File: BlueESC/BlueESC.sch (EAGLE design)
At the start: 36 parts, among them U1 ATMEGA168, U2 V_REG_LDOSMD, Y1 RESONATORSMD

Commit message: Combined logic and power boards into a single board. This is done for several reasons. The first is to create a consistent single schematic to help others view the design. The second is for manufacturing and avoiding double cost of setup.
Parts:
- added C10: 0.1uF, SparkFun-Capacitors:CAP0603-CAP
- added C11, C15, C16, C17: 100uF, SparkFun-Capacitors:CAP_POL7343
- added C2, C3: 1uF, SparkFun-Capacitors:CAP0805
- added C6: 1uF, SparkFun-Capacitors:CAP0603-CAP
- added D1, D2, D3: Schottky, SparkFun-DiscreteSemi:DIODESOD
- added Q1, Q2, Q3: BC817-40W, SparkFun-DiscreteSemi:TRANSISTOR_NPNSOT23
- added Q4, Q5, Q6, Q7, Q8, Q9: SI7370, transistor-fet-bobstarr:SI7370
- added R19, R21, R25, R26, R30, R31: 100, SparkFun-Resistors:33KOHM1/10W1%(0603)
- added R20: 3.3K 1%, SparkFun-Resistors:33KOHM1/10W1%(0603)
- added R22, R27, R32: 10K, SparkFun-Resistors:33KOHM1/10W1%(0603)
- added R23, R28: 2.2K, SparkFun-Resistors:33KOHM1/10W1%(0603)
- added R24, R29: 4.7K, SparkFun-Resistors:33KOHM1/10W1%(0603)
- added R33: 10K NTC, SparkFun-Resistors:33KOHM1/10W1%(0603)
- added R34: 47K, SparkFun:RESISTOR0603-RES
- added R35: 470K, SparkFun:RESISTOR0603-RES
- added U$1, U$2: PADPTH-MED, BR-Eagle-Library:PADPTH-MED
- added U$12, U$13, U$14: PAD1.5X3MM, BR-Eagle-Library:PAD1.5X3MM
- added U$5, U$6, U$7: PAD18AWG, BR-Eagle-Library:PAD18AWG
- added U$8: HEADER-122MM, BR-Eagle-Library:HEADER-122MM
- C1: device SparkFun-Capacitors:CAP0603-CAP -> SparkFun-Capacitors:CAP0805
- R17: value 47K -> 2.2K; device SparkFun:RESISTOR0603-RES -> SparkFun-Resistors:33KOHM1/10W1%(0603)
- R18: value 470K -> 4.7K; device SparkFun:RESISTOR0603-RES -> SparkFun-Resistors:33KOHM1/10W1%(0603)
- U$10: value PAD1.5X3MM -> LOGOBR-LOGO-M; device BR-Eagle-Library:PAD1.5X3MM -> BR-Eagle-Library:LOGOBR-LOGO-M
- U$3: value PAD1.5X3MM -> ACS7XX12-WFQFN; device BR-Eagle-Library:PAD1.5X3MM -> BR-Eagle-Library:ACS7XX12-WFQFN
- U$4: value LOGOBR-LOGO-M -> HEADER-62MM; device BR-Eagle-Library:LOGOBR-LOGO-M -> BR-Eagle-Library:HEADER-62MM
- U$9: value PAD1.5X3MM -> LOGOBR-LOGO-S; device BR-Eagle-Library:PAD1.5X3MM -> BR-Eagle-Library:LOGOBR-LOGO-S
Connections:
- new net GATE_AH: Q4.G, R19.2
- new net GATE_AL: Q5.G, R21.2, R22.2
- new net GATE_BH: Q6.G, R25.2
- new net GATE_BL: Q7.G, R26.2, R27.2
- new net GATE_CH: Q8.G, R30.2
- new net GATE_CL: Q9.G, R31.2, R32.2
- new net L_CURRENT_ADC: R34.1, U$17.4
- new net L_GND: C4.2, C5.2, C6.2, C7.2, C9.-, LED2.C, R11.1, R35.1, R7.1, R8.1, R9.1, U$11.PAD, U$16.1, U$17.1, U$17.12, U$17.2, U1.AGND, U1.GND@1, U1.GND@2, U2.GND, Y1.2
- new net L_PHASE_A: R4.2, U$16.2
- new net L_PHASE_B: R5.2, U$16.3
- new net L_PHASE_C: R6.2, U$16.4
- new net L_PWM_AH: U$17.5, U1.PD2(INT0)
- new net L_PWM_AL: U$17.6, U1.PD3(INT1)
- new net L_PWM_BH: U$17.7, U1.PD4(XCK/T0)
- new net L_PWM_BL: U$17.8, U1.PD5(T1)
- new net L_PWM_CH: U$17.9, U1.PD7(AIN1)
- new net L_PWM_CL: U$17.10, U1.PB3(MOSI/OC2)
- new net L_TEMP_ADC: U$16.5, U1.ADC7
- new net L_VBAT: R10.2, U$17.11, U2.IN
- new net N$12: C3.1, D1.C, R17.2
- new net N$15: C1.1, D2.C, R23.2
- new net N$19: C2.1, D3.C, R28.2
- new net N$2: Q1.B, R18.2
- new net N$4: Q1.C, R17.1, R19.1
- new net N$5: Q2.B, R24.2
- new net N$6: Q2.C, R23.1, R25.1
- new net N$7: Q3.B, R29.2
- new net N$9: Q3.C, R28.1, R30.1
- new net VBAT+: C11.+, C15.+, C16.+, C17.+, U$1.PAD, U$3.IP+1, U$3.IP+2
- new net VCC5V-1: R20.2, U$4.6
- new net VCC5V-2: C10.1, U$3.VCC, U$8.3
- net CURRENT_ADC: now also U$3.VIOUT, U$8.4; no longer R17.1, U$17.4
- net CURRENT_ADC_FILTERED: now also C6.1, R34.2; no longer C1.1, R17.2
- net GND: now also C10.2, C11.-, C15.-, C16.-, C17.-, Q1.E, Q2.E, Q3.E, Q5.S3, Q7.S3, Q9.S3, R22.1, R27.1, R32.1, R33.1, U$2.PAD, U$3.GND, U$4.1, U$8.1, U$8.12, U$8.2; no longer C1.2, C4.2, C5.2, C7.2, C9.-, LED2.C, R11.1, R18.1, R7.1, R8.1, R9.1, U$16.1, U$17.1, U$17.12, U$17.2, U$3.PAD, U1.AGND, U1.GND@1, U1.GND@2, U2.GND, Y1.2
- net PHASE_A: now also C3.2, Q4.S3, Q5.D, U$4.2, U$5.PAD; no longer R4.2, U$16.2
- net PHASE_B: now also C1.2, Q6.S3, Q7.D, U$4.3, U$6.PAD; no longer R5.2, U$16.3
- net PHASE_C: now also C2.2, Q8.S3, Q9.D, U$4.4, U$7.PAD; no longer R6.2, U$16.4
- net PWM: now also R35.2, U$14.PAD; no longer R18.2, U$11.PAD
- net PWM_AH: now also R18.1, U$8.5; no longer U$17.5, U1.PD2(INT0)
- net PWM_AL: now also R21.1, U$8.6; no longer U$17.6, U1.PD3(INT1)
- net PWM_BH: now also R24.1, U$8.7; no longer U$17.7, U1.PD4(XCK/T0)
- net PWM_BL: now also R26.1, U$8.8; no longer U$17.8, U1.PD5(T1)
- net PWM_CH: now also R29.1, U$8.9; no longer U$17.9, U1.PD7(AIN1)
- net PWM_CL: now also R31.1, U$8.10; no longer U$17.10, U1.PB3(MOSI/OC2)
- net SCL: now also U$13.PAD; no longer U$10.PAD
- net SDA: now also U$12.PAD; no longer U$9.PAD
- net TEMP_ADC: now also R20.1, R33.2, U$4.5; no longer U$16.5, U1.ADC7
- net VBAT: now also D1.A, D2.A, D3.A, Q4.D, Q6.D, Q8.D, U$3.IP-1, U$3.IP-2, U$8.11; no longer R10.2, U$17.11, U2.IN
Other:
- note added: "Current Sense"
- note added: "Interface between top and bottom board (ignore for now)"
- note added: "MOSFET Driving"
- note added: "MOSFETs"
- note added: "Motor Pads"
- note added: "Power Decoupling"
- note added: "Power Pads"
- note added: "Temperature Sense"

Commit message: Reorganized combined schematic and broke everything into multiple sheets for easier viewing.
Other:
- note added: "Connections"
- note added: "Control Interface"
- note added: "Current/Voltage/Temp Sensing"
- note added: "Logic Board"
- note added: "Microcontroller"
- note added: "Power"
- note added: "Power Board"
- note removed: "Interface"
- note removed: "Interface between top and bottom board (ignore for now)"
- note removed: "MCU"

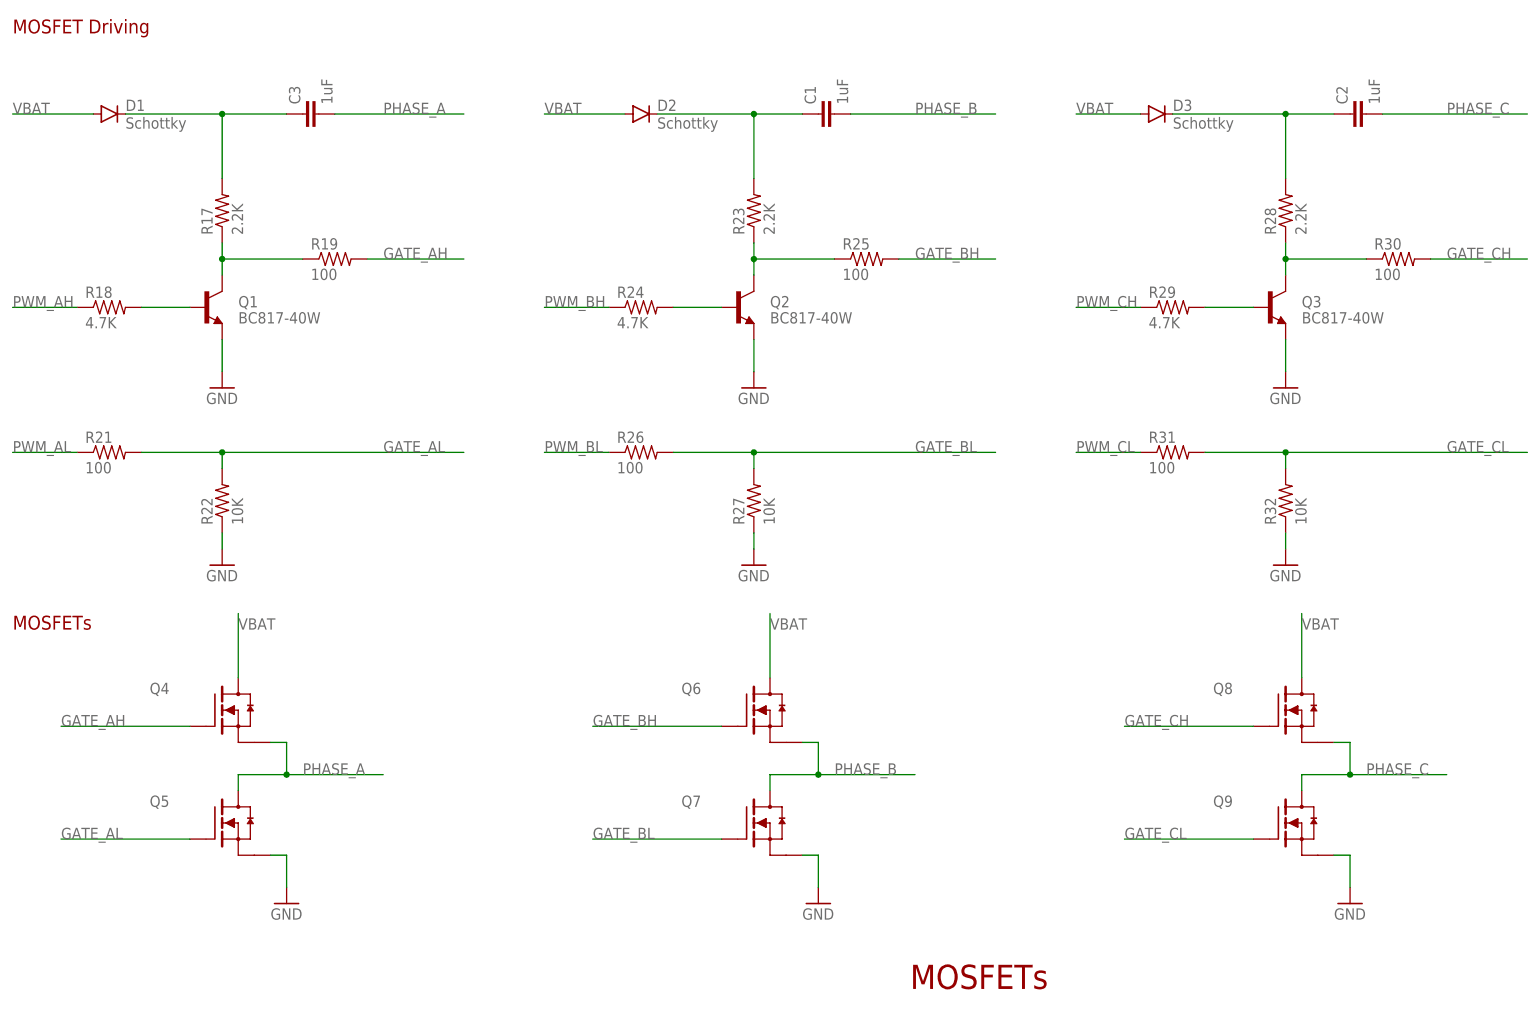
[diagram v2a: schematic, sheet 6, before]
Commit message: Updated MOSFET footprint to TDSON-8 to accommodate new FET and to fix potential soldering errors. This should still fit the SiR158DP as well.
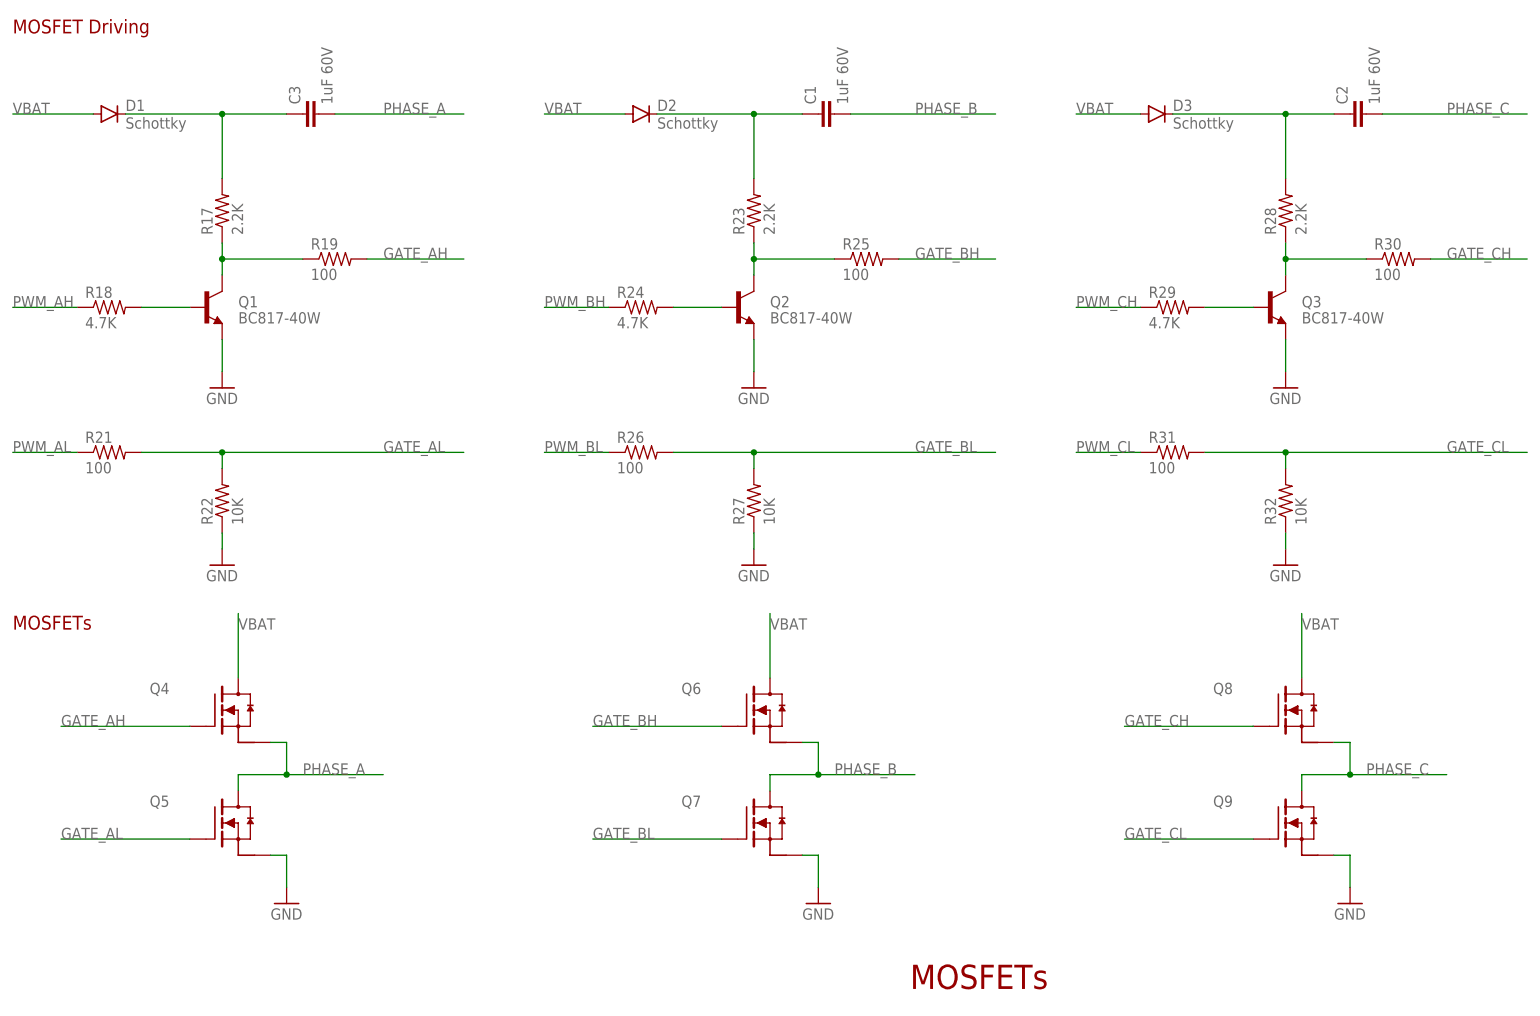
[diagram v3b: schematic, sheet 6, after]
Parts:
- C1, C2, C3: value 1uF -> 1uF 60V
- Q4, Q5, Q6, Q7, Q8, Q9: value SI7370 -> MOSFET-NCHANNEL; device transistor-fet-bobstarr:SI7370 -> BlueRobotics-Main:MOSFET-NCHANNEL
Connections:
- net GND: now also Q5.S, Q7.S, Q9.S; no longer Q5.S3, Q7.S3, Q9.S3
- net PHASE_A: now also Q4.S; no longer Q4.S3
- net PHASE_B: now also Q6.S; no longer Q6.S3
- net PHASE_C: now also Q8.S; no longer Q8.S3
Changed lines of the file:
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@@
 <part name="R32" library="SparkFun-Resistors" deviceset="33KOHM1/10W1%(0603)" device="" value="10K"/>
 <part name="GND16" library="SparkFun" deviceset="GND" device=""/>
-<part name="Q4" library="transistor-fet-bobstarr" deviceset="SI7370" device=""/>
-<part name="Q5" library="transistor-fet-bobstarr" deviceset="SI7370" device=""/>
+<part name="Q4" library="BlueRobotics-Main" deviceset="MOSFET-NCHANNEL" device=""/>
+<part name="Q5" library="BlueRobotics-Main" deviceset="MOSFET-NCHANNEL" device=""/>
 <part name="GND18" library="SparkFun-Aesthetics" deviceset="GND" device=""/>
-<part name="Q6" library="transistor-fet-bobstarr" deviceset="SI7370" device=""/>
-<part name="Q7" library="transistor-fet-bobstarr" deviceset="SI7370" device=""/>
+<part name="Q6" library="BlueRobotics-Main" deviceset="MOSFET-NCHANNEL" device=""/>
+<part name="Q7" library="BlueRobotics-Main" deviceset="MOSFET-NCHANNEL" device=""/>
 <part name="GND19" library="SparkFun-Aesthetics" deviceset="GND" device=""/>
-<part name="Q8" library="transistor-fet-bobstarr" deviceset="SI7370" device=""/>
-<part name="Q9" library="transistor-fet-bobstarr" deviceset="SI7370" device=""/>
+<part name="Q8" library="BlueRobotics-Main" deviceset="MOSFET-NCHANNEL" device=""/>
+<part name="Q9" library="BlueRobotics-Main" deviceset="MOSFET-NCHANNEL" device=""/>
 <part name="GND20" library="SparkFun-Aesthetics" deviceset="GND" device=""/>
 <part name="C15" library="SparkFun-Capacitors" deviceset="CAP_POL" device="7343" value="100uF"/>
@@
 <part name="D2" library="SparkFun-DiscreteSemi" deviceset="DIODE" device="SOD" value="Schottky"/>
 <part name="D3" library="SparkFun-DiscreteSemi" deviceset="DIODE" device="SOD" value="Schottky"/>
-<part name="C1" library="SparkFun-Capacitors" deviceset="CAP" device="0805" value="1uF"/>
-<part name="C2" library="SparkFun-Capacitors" deviceset="CAP" device="0805" value="1uF"/>
-<part name="C3" library="SparkFun-Capacitors" deviceset="CAP" device="0805" value="1uF"/>
+<part name="C1" library="SparkFun-Capacitors" deviceset="CAP" device="0805" value="1uF 60V"/>
+<part name="C2" library="SparkFun-Capacitors" deviceset="CAP" device="0805" value="1uF 60V"/>
+<part name="C3" library="SparkFun-Capacitors" deviceset="CAP" device="0805" value="1uF 60V"/>
 <part name="GND2" library="SparkFun-Aesthetics" deviceset="GND" device=""/>
 <part name="C10" library="SparkFun-Capacitors" deviceset="CAP" device="0603-CAP" value="0.1uF"/>
@@
 <net name="GND" class="0">
 <segment>
-<pinref part="Q5" gate="G$1" pin="S3"/>
+<pinref part="Q5" gate="G$1" pin="S"/>
 <pinref part="GND18" gate="1" pin="GND"/>
 <wire x1="48.26" y1="48.26" x2="50.8" y2="48.26" width="0.1524" layer="91"/>
@@
 </segment>
 <segment>
-<pinref part="Q7" gate="G$1" pin="S3"/>
+<pinref part="Q7" gate="G$1" pin="S"/>
 <pinref part="GND19" gate="1" pin="GND"/>
 <wire x1="132.08" y1="48.26" x2="134.62" y2="48.26" width="0.1524" layer="91"/>
@@
 </segment>
 <segment>
-<pinref part="Q9" gate="G$1" pin="S3"/>
+<pinref part="Q9" gate="G$1" pin="S"/>
 <pinref part="GND20" gate="1" pin="GND"/>
 <wire x1="215.9" y1="48.26" x2="218.44" y2="48.26" width="0.1524" layer="91"/>
@@
 <wire x1="43.18" y1="58.42" x2="43.18" y2="60.96" width="0.1524" layer="91"/>
 <wire x1="43.18" y1="60.96" x2="50.8" y2="60.96" width="0.1524" layer="91"/>
-<pinref part="Q4" gate="G$1" pin="S3"/>
+<pinref part="Q4" gate="G$1" pin="S"/>
 <wire x1="50.8" y1="60.96" x2="66.04" y2="60.96" width="0.1524" layer="91"/>
 <wire x1="48.26" y1="66.04" x2="50.8" y2="66.04" width="0.1524" layer="91"/>
@@
 <wire x1="127" y1="58.42" x2="127" y2="60.96" width="0.1524" layer="91"/>
 <wire x1="127" y1="60.96" x2="134.62" y2="60.96" width="0.1524" layer="91"/>
-<pinref part="Q6" gate="G$1" pin="S3"/>
+<pinref part="Q6" gate="G$1" pin="S"/>
 <wire x1="134.62" y1="60.96" x2="149.86" y2="60.96" width="0.1524" layer="91"/>
 <wire x1="132.08" y1="66.04" x2="134.62" y2="66.04" width="0.1524" layer="91"/>
@@
 <wire x1="210.82" y1="58.42" x2="210.82" y2="60.96" width="0.1524" layer="91"/>
 <wire x1="210.82" y1="60.96" x2="218.44" y2="60.96" width="0.1524" layer="91"/>
-<pinref part="Q8" gate="G$1" pin="S3"/>
+<pinref part="Q8" gate="G$1" pin="S"/>
 <wire x1="218.44" y1="60.96" x2="233.68" y2="60.96" width="0.1524" layer="91"/>
 <wire x1="215.9" y1="66.04" x2="218.44" y2="66.04" width="0.1524" layer="91"/>

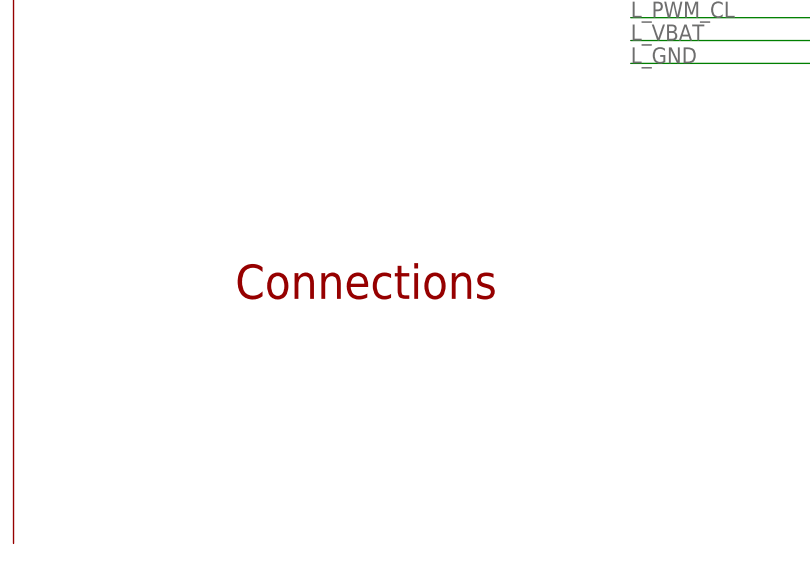
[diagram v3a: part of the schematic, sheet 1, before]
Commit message: Updated schematic sheets to use the new BR frame.
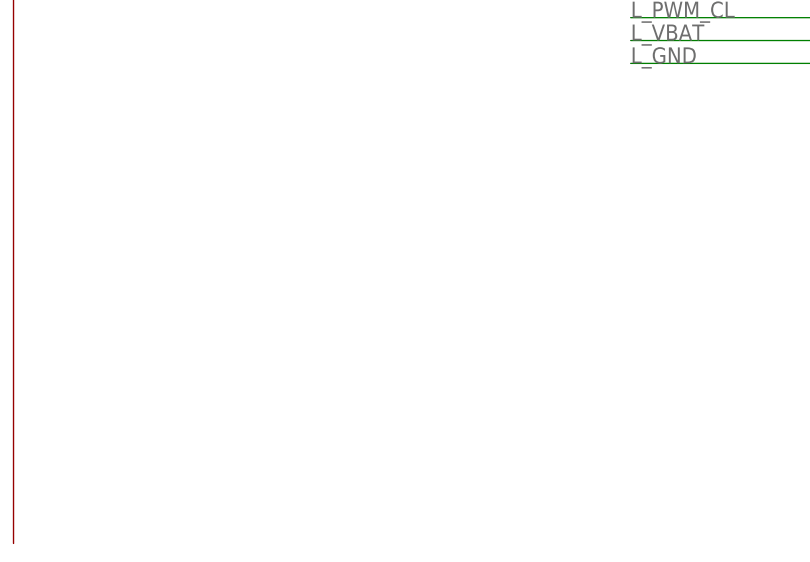
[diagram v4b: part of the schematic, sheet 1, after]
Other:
- note removed: "Connections"
- note removed: "Current/Voltage/Temp Sensing"
- note removed: "Microcontroller"
- note removed: "Power"
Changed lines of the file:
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@@
 <part name="R35" library="SparkFun" deviceset="RESISTOR" device="0603-RES" value="470K"/>
 <part name="GND10" library="SparkFun" deviceset="GND" device=""/>
-<part name="FRAME5" library="frames" deviceset="LETTER_L" device=""/>
-<part name="FRAME1" library="frames" deviceset="LETTER_L" device=""/>
-<part name="FRAME2" library="frames" deviceset="LETTER_L" device=""/>
-<part name="FRAME3" library="frames" deviceset="LETTER_L" device=""/>
-<part name="FRAME4" library="frames" deviceset="LETTER_L" device=""/>
-<part name="FRAME6" library="frames" deviceset="LETTER_L" device=""/>
+<part name="FRAME5" library="BlueRobotics-Main" deviceset="FRAME-BLUEROBOTICS" device="" value="Connectors &amp; Interfaces"/>
+<part name="FRAME1" library="BlueRobotics-Main" deviceset="FRAME-BLUEROBOTICS" device="" value="Current/Voltage/Temp Sensing"/>
+<part name="FRAME2" library="BlueRobotics-Main" deviceset="FRAME-BLUEROBOTICS" device="" value="MOSFETs and Switching Circuitry"/>
+<part name="FRAME3" library="BlueRobotics-Main" deviceset="FRAME-BLUEROBOTICS" device="" value="Phase Sensing"/>
+<part name="FRAME4" library="BlueRobotics-Main" deviceset="FRAME-BLUEROBOTICS" device="" value="Microcontroller, LEDs, and Misc."/>
+<part name="FRAME6" library="BlueRobotics-Main" deviceset="FRAME-BLUEROBOTICS" device="" value="Main Power Caps and 5V Power"/>
 </parts>
 <sheets>
@@
 <text x="12.7" y="134.62" size="2.1844" layer="94">Motor Pads</text>
 <text x="12.7" y="96.52" size="2.1844" layer="94">Interface between top and bottom board</text>
-<text x="149.098" y="27.178" size="3.81" layer="94">Connections</text>
 <wire x1="124.46" y1="185.42" x2="124.46" y2="0" width="0.1524" layer="94"/>
 <text x="134.62" y="137.16" size="1.778" layer="94">Control Interface</text>
@@
 <sheet>
 <plain>
-<text x="149.098" y="27.178" size="3.81" layer="94">Microcontroller</text>
 <wire x1="17.78" y1="109.728" x2="17.78" y2="109.22" width="0.2032" layer="97"/>
 <text x="63.754" y="152.908" size="1.778" layer="97">ATMEGA8A</text>
@@
 <sheet>
 <plain>
-<text x="149.098" y="27.178" size="3.81" layer="94">Current/Voltage/Temp Sensing</text>
 <wire x1="124.46" y1="185.42" x2="124.46" y2="0" width="0.1524" layer="94"/>
 <text x="2.54" y="177.8" size="3.81" layer="94">Power Board</text>
@@
 <sheet>
 <plain>
-<text x="149.098" y="27.178" size="3.81" layer="94">Power</text>
 <wire x1="124.46" y1="185.42" x2="124.46" y2="0" width="0.1524" layer="94"/>
 <text x="2.54" y="177.8" size="3.81" layer="94">Power Board</text>
@@
 <sheet>
 <plain>
-<text x="149.098" y="27.178" size="3.81" layer="94">Phase Sensing</text>
 <text x="58.42" y="137.16" size="2.1844" layer="94">Phase Sensing</text>
 </plain>
@@
 <sheet>
 <plain>
-<text x="149.098" y="27.178" size="3.81" layer="94">MOSFETs</text>
 <text x="7.62" y="83.82" size="2.1844" layer="94">MOSFETs</text>
 <text x="7.62" y="177.8" size="2.1844" layer="94">MOSFET Driving</text>
